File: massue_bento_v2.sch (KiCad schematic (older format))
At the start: 26 parts, among them K1 CONN_3, K2 CONN_3, K3 CONN_3, P1 TST, P2 TST, P3 SWD_CONN, P4 CONN_4, P5 TST, P6 TST, P7 TST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

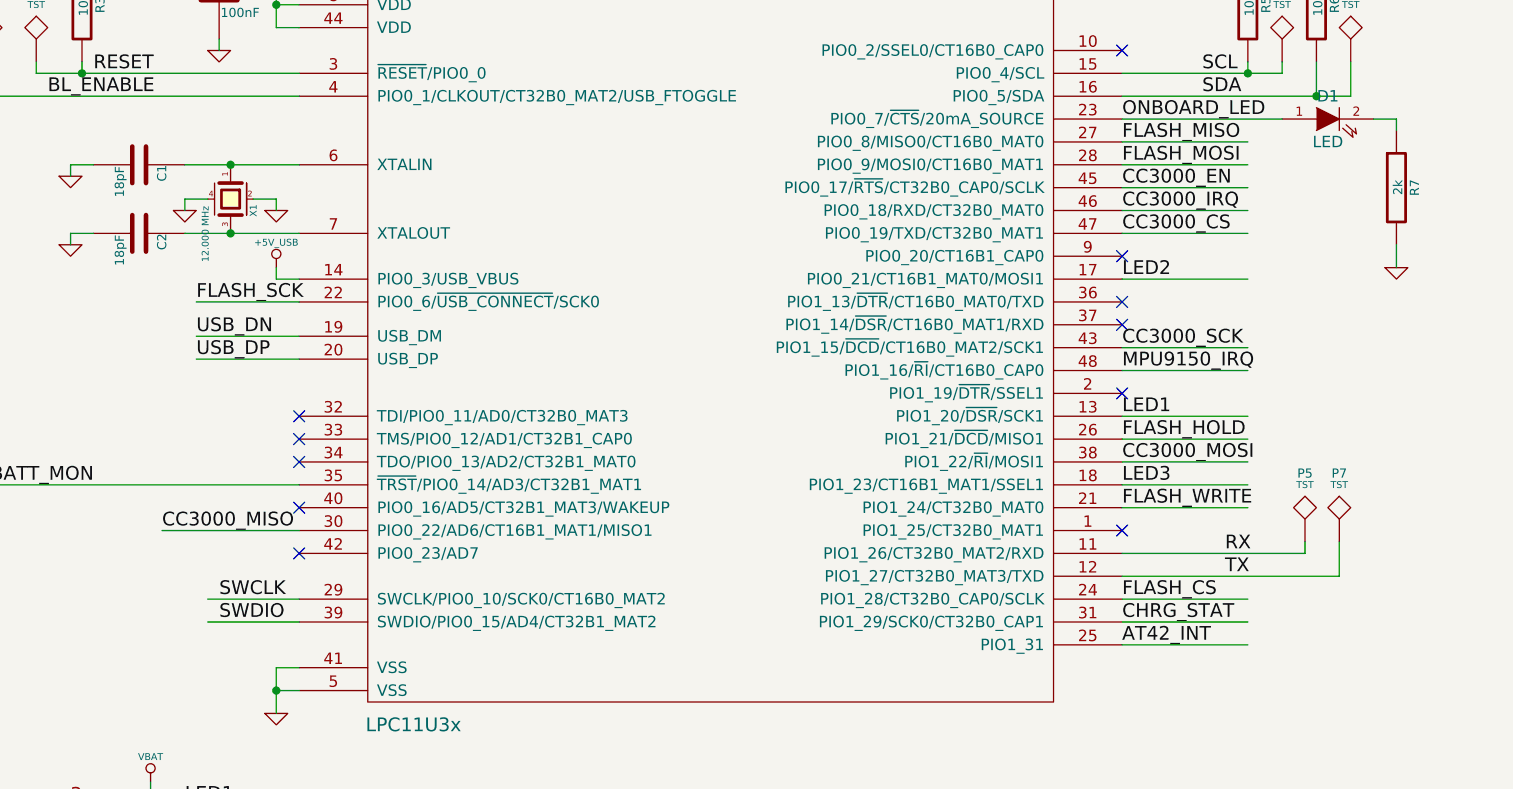
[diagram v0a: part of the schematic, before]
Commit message: Finished routing of signals, re-organization of power
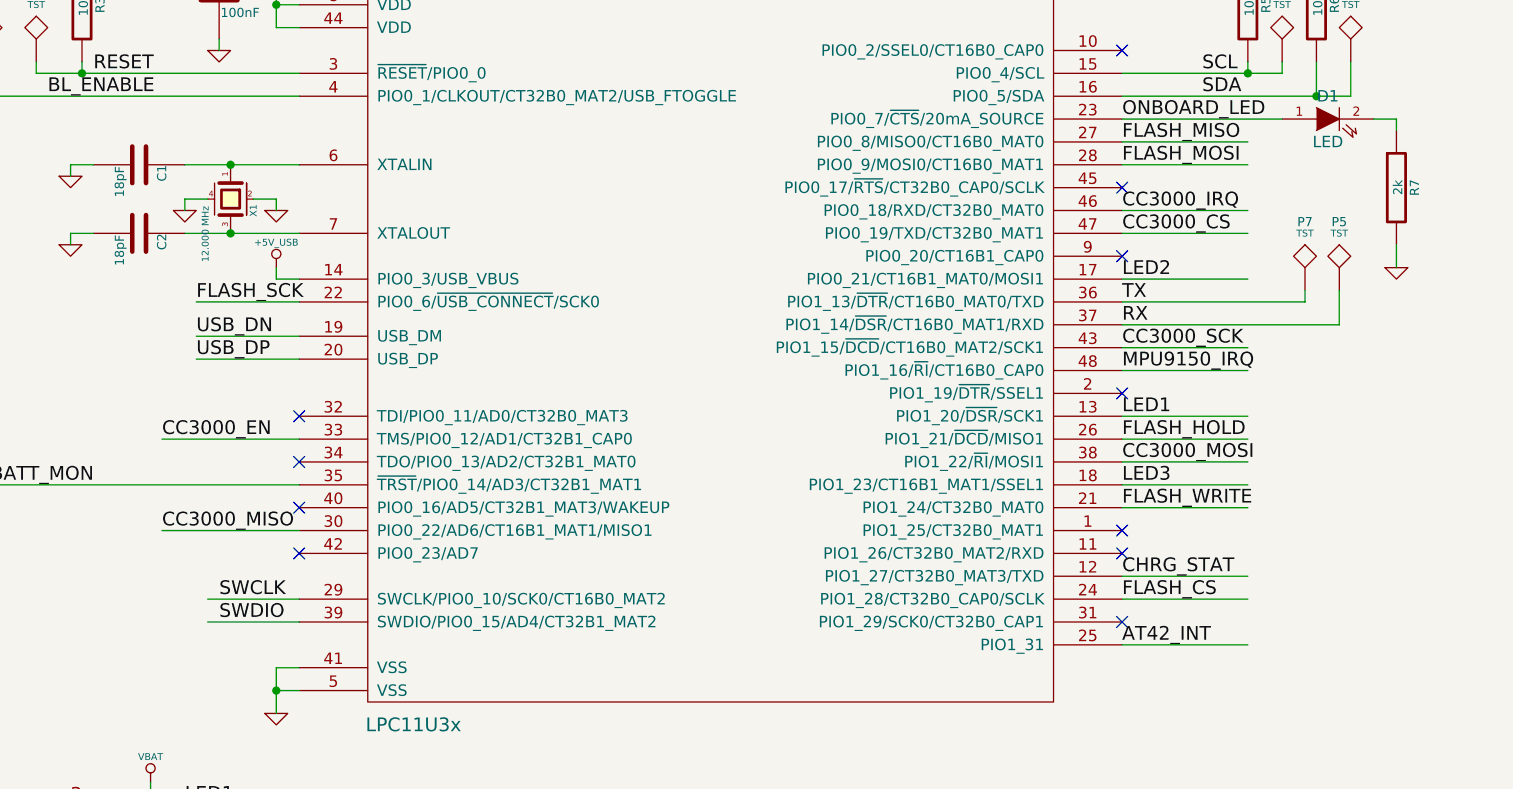
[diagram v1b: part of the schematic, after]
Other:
- moved on the sheet: P5, P7
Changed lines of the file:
@@
 Wire Wire Line
 	6250 1950 6950 1950
-Wire Wire Line
-	6250 3950 7200 3950
-Wire Wire Line
-	6250 3850 7050 3850
-Wire Wire Line
-	7200 3950 7200 3800
-Text Label 6700 3950 0    60   ~ 0
+Text Label 6250 2750 0    60   ~ 0
 TX
-Text Label 6700 3850 0    60   ~ 0
+Text Label 6250 2850 0    60   ~ 0
 RX
 $Comp
@@
 L TST P7
 U 1 1 53A6533B
-P 7200 3800
-F 0 "P7" H 7200 4100 40  0000 C CNN
-F 1 "TST" H 7200 4050 30  0000 C CNN
-F 2 "" H 7200 3800 60  0000 C CNN
-F 3 "" H 7200 3800 60  0000 C CNN
-	1    7200 3800
+P 7050 2700
+F 0 "P7" H 7050 3000 40  0000 C CNN
+F 1 "TST" H 7050 2950 30  0000 C CNN
+F 2 "" H 7050 2700 60  0000 C CNN
+F 3 "" H 7050 2700 60  0000 C CNN
+	1    7050 2700
 	1    0    0    -1
 $EndComp
@@
 L TST P5
 U 1 1 53A652B6
-P 7050 3800
-F 0 "P5" H 7050 4100 40  0000 C CNN
-F 1 "TST" H 7050 4050 30  0000 C CNN
-F 2 "" H 7050 3800 60  0000 C CNN
-F 3 "" H 7050 3800 60  0000 C CNN
-	1    7050 3800
+P 7200 2700
+F 0 "P5" H 7200 3000 40  0000 C CNN
+F 1 "TST" H 7200 2950 30  0000 C CNN
+F 2 "" H 7200 2700 60  0000 C CNN
+F 3 "" H 7200 2700 60  0000 C CNN
+	1    7200 2700
 	1    0    0    -1
 $EndComp
@@
 Wire Wire Line
 	6250 2150 6800 2150
-Wire Wire Line
-	6250 4150 6800 4150
 Text Label 2050 3750 0    60   ~ 0
 CC3000_MISO
@@
 CHRG_STAT
 Wire Wire Line
-	6250 2250 6800 2250
-Wire Wire Line
 	6250 2350 6800 2350
 Wire Wire Line
 	6250 2450 6800 2450
-Text Label 6250 2250 0    60   ~ 0
+Text Label 2050 3350 0    60   ~ 0
 CC3000_EN
 Text Label 6250 2350 0    60   ~ 0
@@
 Text Label 6250 3350 0    60   ~ 0
 FLASH_HOLD
-Text Label 6250 4150 0    60   ~ 0
+Text Label 6250 3950 0    60   ~ 0
 CHRG_STAT
 $Comp
@@
 F7 "CC3000_SW_EN" I L 9300 3050 60
 $EndSheet
-Wire Wire Line
-	7050 3850 7050 3800
 $Comp
 L VBAT #PWR028
@@
 Wire Wire Line
 	6250 3550 6800 3550
-NoConn ~ 2650 3350
+NoConn ~ 6250 2250
 NoConn ~ 2650 3650
 NoConn ~ 2650 3850
-NoConn ~ 6250 2750
-NoConn ~ 6250 2850
+NoConn ~ 6250 3850
+NoConn ~ 6250 4150
 Wire Wire Line
 	6250 3050 6800 3050
+Wire Wire Line
+	6250 2750 7050 2750
+Wire Wire Line
+	7050 2750 7050 2700
+Wire Wire Line
+	6250 2850 7200 2850
+Wire Wire Line
+	7200 2850 7200 2700
+Wire Wire Line
+	6250 3950 6800 3950
+Wire Wire Line
+	2050 3350 2650 3350
 $EndSCHEMATC

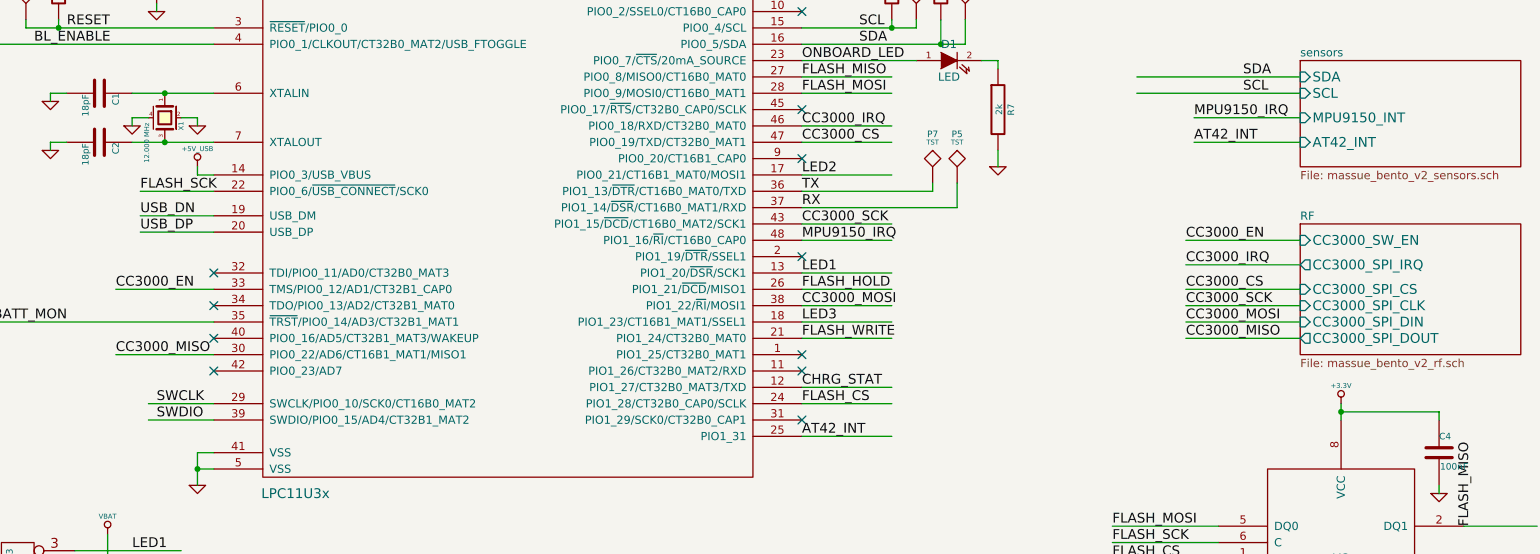
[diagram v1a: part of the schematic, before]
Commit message: Changed MS5607 altimeter for MPL3115A2
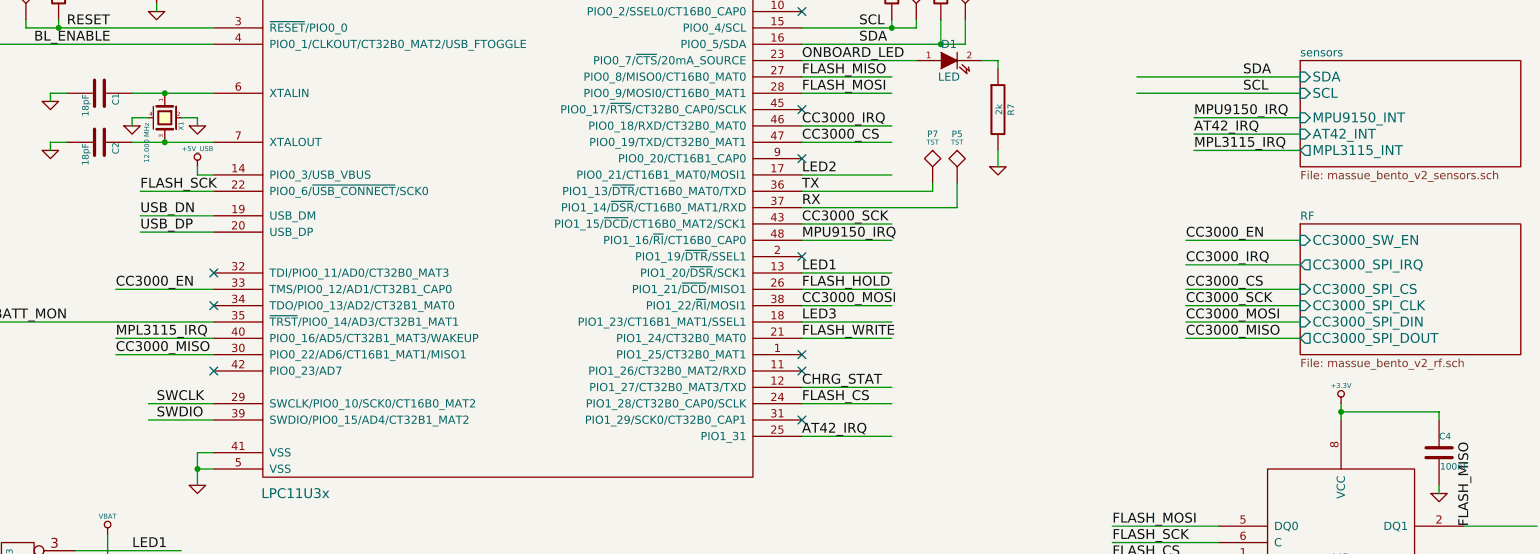
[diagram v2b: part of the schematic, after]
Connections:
- net labels added: AT42_IRQ, MPL3115_IRQ
- net labels removed: AT42_INT
- wire segments 123 -> 125
- no-connect marks 12 -> 11
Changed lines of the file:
@@
 F3 "SCL" I L 9300 2150 60
 F4 "MPU9150_INT" I L 9300 2300 60
-F5 "AT42_INT" I L 9300 2450 60
+F5 "AT42_INT" I L 9300 2400 60
+F6 "MPL3115_INT" O L 9300 2500 60
 $EndSheet
 $Comp
@@
 Text Label 6250 3050 0    60   ~ 0
 MPU9150_IRQ
-Wire Wire Line
-	9300 2450 8650 2450
-Text Label 8650 2450 0    60   ~ 0
-AT42_INT
+Text Label 8650 2400 0    60   ~ 0
+AT42_IRQ
 Wire Wire Line
 	6250 4250 6800 4250
 Text Label 6250 4250 0    60   ~ 0
-AT42_INT
+AT42_IRQ
 Wire Wire Line
 	2650 2750 2200 2750
@@
 	6250 3550 6800 3550
 NoConn ~ 6250 2250
-NoConn ~ 2650 3650
 NoConn ~ 2650 3850
 NoConn ~ 6250 3850
@@
 Wire Wire Line
 	2050 3350 2650 3350
+Wire Wire Line
+	8650 2400 9300 2400
+Wire Wire Line
+	9300 2500 8650 2500
+Text Label 8650 2500 0    60   ~ 0
+MPL3115_IRQ
+Wire Wire Line
+	2050 3650 2650 3650
+Text Label 2050 3650 0    60   ~ 0
+MPL3115_IRQ
 $EndSCHEMATC

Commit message: Clean: same value for 100nF/0.1uf capacitors, re-organization of labels, add dimension labels
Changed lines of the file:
@@
 F2 "SDA" I L 9300 2050 60
 F3 "SCL" I L 9300 2150 60
-F4 "MPU9150_INT" I L 9300 2300 60
-F5 "AT42_INT" I L 9300 2400 60
+F4 "MPU9150_INT" O L 9300 2300 60
+F5 "AT42_INT" O L 9300 2400 60
 F6 "MPL3115_INT" O L 9300 2500 60
 $EndSheet
@@
 Wire Wire Line
 	10300 4800 10750 4800
-Text Label 10350 4800 1    60   ~ 0
+Text Label 10300 4800 0    60   ~ 0
 FLASH_MISO
 Wire Wire Line
